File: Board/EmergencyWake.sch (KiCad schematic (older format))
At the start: 125 parts, among them J1 USB_C_Plug_USB2.0, J2 Micro_SD_Card_Det, J3 Conn_01x03, J4 Conn_01x02, J5 Conn_01x03, J6 Conn_01x04, J7 Conn_01x02, J8 Conn_01x04, J9 Conn_01x04, Q1 AO3400A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

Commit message: [Board] Added logo and changed USB plug type
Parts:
- removed J1: USB_C_Plug_USB2.0, Wuerth:632723300011, symbol Connector:USB_C_Plug_USB2.0
- added J1: USB_C_Receptacle_USB2.0, Wuerth:632723300011, symbol Connector:USB_C_Receptacle_USB2.0
- added R43: 5.1k, Resistor_SMD:R_0603_1608Metric, symbol Device:R
- R6: value 100k -> 5.1k; footprint Resistor_SMD:R_0402_1005Metric -> Resistor_SMD:R_0603_1608Metric; LCSC C25741 -> C23186
- R7: footprint Resistor_SMD:R_0402_1005Metric -> Resistor_SMD:R_0603_1608Metric; LCSC C25867 -> C22843
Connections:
- wire segments 535 -> 543
- no-connect marks 57 -> 58
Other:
- moved on the sheet: Q1, R11, R7, TP1, TP2
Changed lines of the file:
@@
 L power:GND #PWR08
 U 1 1 5E2C0277
-P 2800 5300
-F 0 "#PWR08" H 2800 5050 50  0001 C CNN
-F 1 "GND" H 2805 5127 50  0000 C CNN
-F 2 "" H 2800 5300 50  0001 C CNN
-F 3 "" H 2800 5300 50  0001 C CNN
-	1    2800 5300
+P 2800 5200
+F 0 "#PWR08" H 2800 4950 50  0001 C CNN
+F 1 "GND" H 2805 5027 50  0000 C CNN
+F 2 "" H 2800 5200 50  0001 C CNN
+F 3 "" H 2800 5200 50  0001 C CNN
+	1    2800 5200
 	1    0    0    -1
 $EndComp
@@
 L Device:Q_NMOS_GSD Q1
 U 1 1 5E31A1D8
-P 2900 4800
-F 0 "Q1" H 2750 4650 50  0000 L CNN
-F 1 "AO3400A" H 2550 4550 50  0000 L CNN
-F 2 "Package_TO_SOT_SMD:SOT-23" H 3100 4900 50  0001 C CNN
-F 3 "https://datasheet.lcsc.com/szlcsc/Alpha-Omega-Semicon-AOS-AO3400A_C20917.pdf" H 2900 4800 50  0001 C CNN
-F 4 "C20917" H 2900 4800 50  0001 C CNN "LCSC"
-	1    2900 4800
+P 2900 4700
+F 0 "Q1" H 2750 4550 50  0000 L CNN
+F 1 "AO3400A" H 2550 4450 50  0000 L CNN
+F 2 "Package_TO_SOT_SMD:SOT-23" H 3100 4800 50  0001 C CNN
+F 3 "https://datasheet.lcsc.com/szlcsc/Alpha-Omega-Semicon-AOS-AO3400A_C20917.pdf" H 2900 4700 50  0001 C CNN
+F 4 "C20917" H 2900 4700 50  0001 C CNN "LCSC"
+	1    2900 4700
 	-1   0    0    -1
 $EndComp
@@
 	2550 4100 2800 4100
 Wire Wire Line
-	2800 4100 2800 4600
+	2800 4100 2800 4500
 Wire Wire Line
-	2800 5000 2800 5200
+	2800 4900 2800 5100
 Wire Wire Line
-	2550 4400 2650 4400
+	2650 5100 2800 5100
+Connection ~ 2800 5100
 Wire Wire Line
-	2650 4400 2650 5200
-Wire Wire Line
-	2650 5200 2800 5200
-Connection ~ 2800 5200
-Wire Wire Line
-	2800 5200 2800 5300
-Wire Wire Line
-	2550 4500 4950 4500
+	2800 5100 2800 5200
 Wire Wire Line
 	2550 3900 2650 3900
@@
 $EndComp
 Wire Wire Line
-	3100 4800 3400 4800
+	3100 4700 3400 4700
 $Comp
 L power:GND #PWR03
@@
 $EndComp
 Wire Wire Line
-	2800 5200 3400 5200
+	2800 5100 3400 5100
 Wire Wire Line
-	3400 5200 3400 5150
+	3400 5100 3400 5050
 Wire Wire Line
-	3400 4850 3400 4800
-Connection ~ 3400 4800
+	3400 4750 3400 4700
+Connection ~ 3400 4700
 Wire Wire Line
-	3400 4800 4950 4800
-Text Label 4950 4800 2    50   ~ 0
+	3400 4700 4950 4700
+Text Label 4950 4700 2    50   ~ 0
 SD_EN
-Text Label 4950 4500 2    50   ~ 0
+Text Label 4950 4400 2    50   ~ 0
 SD_DET
 $Comp
@@
 L Device:R R11
 U 1 1 5E33508E
-P 3400 5000
-F 0 "R11" H 3470 5046 50  0000 L CNN
-F 1 "100k" H 3470 4955 50  0000 L CNN
-F 2 "Resistor_SMD:R_0402_1005Metric" V 3330 5000 50  0001 C CNN
-F 3 "~" H 3400 5000 50  0001 C CNN
-F 4 "C25741" H 3400 5000 50  0001 C CNN "LCSC"
-	1    3400 5000
+P 3400 4900
+F 0 "R11" H 3470 4946 50  0000 L CNN
+F 1 "100k" H 3470 4855 50  0000 L CNN
+F 2 "Resistor_SMD:R_0402_1005Metric" V 3330 4900 50  0001 C CNN
+F 3 "~" H 3400 4900 50  0001 C CNN
+F 4 "C25741" H 3400 4900 50  0001 C CNN "LCSC"
+	1    3400 4900
 	1    0    0    -1
 $EndComp
@@
 L Connector:TestPoint TP1
 U 1 1 5E3C768F
-P 1950 800
-F 0 "TP1" H 2008 918 50  0000 L CNN
-F 1 "5V in" H 2008 827 50  0000 L CNN
-F 2 "TestPoint:TestPoint_Loop_D1.80mm_Drill1.0mm_Beaded" H 2150 800 50  0001 C CNN
-F 3 "~" H 2150 800 50  0001 C CNN
-	1    1950 800
+P 2050 800
+F 0 "TP1" H 2108 918 50  0000 L CNN
+F 1 "5V in" H 2108 827 50  0000 L CNN
+F 2 "TestPoint:TestPoint_Loop_D1.80mm_Drill1.0mm_Beaded" H 2250 800 50  0001 C CNN
+F 3 "~" H 2250 800 50  0001 C CNN
+	1    2050 800
 	1    0    0    -1
 $EndComp
@@
 L Connector:TestPoint TP2
 U 1 1 5E3C8161
-P 2600 2500
-F 0 "TP2" H 2658 2618 50  0000 L CNN
-F 1 "GND in" H 2658 2527 50  0000 L CNN
-F 2 "TestPoint:TestPoint_Loop_D1.80mm_Drill1.0mm_Beaded" H 2800 2500 50  0001 C CNN
-F 3 "~" H 2800 2500 50  0001 C CNN
-	1    2600 2500
-	1    0    0    -1
-$EndComp
-$Comp
-L Connector:USB_C_Plug_USB2.0 J1
-U 1 1 5E43077B
-P 1200 1550
-F 0 "J1" H 1307 2417 50  0000 C CNN
-F 1 "USB_C_Plug_USB2.0" H 1307 2326 50  0000 C CNN
-F 2 "Wuerth:632723300011" H 1350 1550 50  0001 C CNN
-F 3 "https://www.we-online.de/katalog/datasheet/632723300011.pdf" H 1350 1550 50  0001 C CNN
-F 4 "632723300011" H 1200 1550 50  0001 C CNN "Würth"
-	1    1200 1550
+P 2750 2500
+F 0 "TP2" H 2808 2618 50  0000 L CNN
+F 1 "GND in" H 2808 2527 50  0000 L CNN
+F 2 "TestPoint:TestPoint_Loop_D1.80mm_Drill1.0mm_Beaded" H 2950 2500 50  0001 C CNN
+F 3 "~" H 2950 2500 50  0001 C CNN
+	1    2750 2500
 	1    0    0    -1
 $EndComp
-NoConn ~ 1800 1250
 $Comp
 L Device:R R6
@@
 P 1950 1900
 F 0 "R6" H 2020 1946 50  0000 L CNN
-F 1 "100k" H 2020 1855 50  0000 L CNN
-F 2 "Resistor_SMD:R_0402_1005Metric" V 1880 1900 50  0001 C CNN
+F 1 "5.1k" H 2020 1855 50  0000 L CNN
+F 2 "Resistor_SMD:R_0603_1608Metric" V 1880 1900 50  0001 C CNN
 F 3 "~" H 1950 1900 50  0001 C CNN
-F 4 "C25741" H 1950 1900 50  0001 C CNN "LCSC"
+F 4 "C23186" H 1950 1900 50  0001 C CNN "LCSC"
 	1    1950 1900
 	1    0    0    -1
@@
 Connection ~ 3150 850
 Wire Wire Line
-	2500 950  1950 950
+	2500 950  2050 950
 Wire Wire Line
 	3150 1500 3150 2500
 Wire Wire Line
-	3150 2500 2600 2500
+	3150 2500 2750 2500
 Connection ~ 1950 2500
 Wire Wire Line
-	1800 1450 2950 1450
+	1800 1450 1850 1450
 Wire Wire Line
-	1800 1650 2350 1650
+	1800 1650 1850 1650
 Wire Wire Line
 	1200 2500 1700 2500
@@
 	1700 2500 1950 2500
 Wire Wire Line
-	1950 800  1950 950
+	2050 800  2050 950
 Wire Wire Line
 	2900 850  3150 850
-Connection ~ 1950 950
+Connection ~ 2050 950
 Wire Wire Line
-	1950 950  1800 950
-Connection ~ 2600 2500
+	2050 950  1800 950
+Connection ~ 2750 2500
 Wire Wire Line
-	2600 2500 1950 2500
+	2750 2500 2250 2500
 Text Label 2950 1650 2    50   ~ 0
 USB_DP
@@
 L Device:R R7
 U 1 1 5EAA5F48
-P 2350 1900
-F 0 "R7" H 2420 1946 50  0000 L CNN
-F 1 "1.5k" H 2420 1855 50  0000 L CNN
-F 2 "Resistor_SMD:R_0402_1005Metric" V 2280 1900 50  0001 C CNN
-F 3 "~" H 2350 1900 50  0001 C CNN
-F 4 "C25867" H 2350 1900 50  0001 C CNN "LCSC"
-	1    2350 1900
+P 2550 1900
+F 0 "R7" H 2620 1946 50  0000 L CNN
+F 1 "1.5k" H 2620 1855 50  0000 L CNN
+F 2 "Resistor_SMD:R_0603_1608Metric" V 2480 1900 50  0001 C CNN
+F 3 "~" H 2550 1900 50  0001 C CNN
+F 4 "C22843" H 2550 1900 50  0001 C CNN "LCSC"
+	1    2550 1900
 	1    0    0    -1
 $EndComp
 Wire Wire Line
-	2350 1750 2350 1650
-Connection ~ 2350 1650
+	2550 1750 2550 1650
+Connection ~ 2550 1650
 Wire Wire Line
-	2350 1650 2950 1650
+	2550 1650 2950 1650
 $Comp
 L power:VCC #PWR06
 U 1 1 5EADF0A8
-P 2350 2100
-F 0 "#PWR06" H 2350 1950 50  0001 C CNN
-F 1 "VCC" H 2367 2273 50  0000 C CNN
-F 2 "" H 2350 2100 50  0001 C CNN
-F 3 "" H 2350 2100 50  0001 C CNN
-	1    2350 2100
+P 2550 2100
+F 0 "#PWR06" H 2550 1950 50  0001 C CNN
+F 1 "VCC" H 2550 2250 50  0000 C CNN
+F 2 "" H 2550 2100 50  0001 C CNN
+F 3 "" H 2550 2100 50  0001 C CNN
+	1    2550 2100
 	-1   0    0    1
 $EndComp
 Wire Wire Line
-	2350 2050 2350 2100
+	2550 2050 2550 2100
 $Comp
 L power:+5V #PWR021
@@
 Connection ~ 10800 1050
 Wire Wire Line
-	9250 1950 10100 1950
-Wire Wire Line
 	10800 1950 10800 1850
 Wire Wire Line
-	10300 1800 10300 1950
-Connection ~ 10300 1950
-Wire Wire Line
-	10300 1950 10800 1950
-Wire Wire Line
-	10100 1800 10100 1950
-Connection ~ 10100 1950
+	10200 1800 10200 1950
+Connection ~ 10200 1950
 Wire Wire Line
-	10100 1950 10300 1950
+	10200 1950 10800 1950
 Wire Wire Line
 	9250 1850 9250 1950
@@
 	1    0    0    -1
 $EndComp
+Wire Wire Line
+	9250 1950 10200 1950
+Wire Wire Line
+	2550 4500 2650 4500
+Wire Wire Line
+	2650 4500 2650 5100
+Wire Wire Line
+	4950 4400 2550 4400
+$Comp
+L Connector:USB_C_Receptacle_USB2.0 J1
+U 1 1 5E98AED3
+P 1200 1550
+F 0 "J1" H 1307 2417 50  0000 C CNN
+F 1 "USB_C_Receptacle_USB2.0" H 1307 2326 50  0000 C CNN
+F 2 "Wuerth:632723300011" H 1350 1550 50  0001 C CNN
+F 3 "https://www.usb.org/sites/default/files/documents/usb_type-c.zip" H 1350 1550 50  0001 C CNN
+	1    1200 1550
+	1    0    0    -1
+$EndComp
+Wire Wire Line
+	1800 1550 1850 1550
+Wire Wire Line
+	1850 1550 1850 1450
+Connection ~ 1850 1450
+Wire Wire Line
+	1850 1450 2950 1450
+Wire Wire Line
+	1800 1750 1850 1750
+Wire Wire Line
+	1850 1750 1850 1650
+Connection ~ 1850 1650
+Wire Wire Line
+	1850 1650 2550 1650
+$Comp
+L Device:R R43
+U 1 1 5EB8A4F4
+P 2250 1900
+F 0 "R43" H 2320 1946 50  0000 L CNN
+F 1 "5.1k" H 2320 1855 50  0000 L CNN
+F 2 "Resistor_SMD:R_0603_1608Metric" V 2180 1900 50  0001 C CNN
+F 3 "~" H 2250 1900 50  0001 C CNN
+F 4 "C23186" H 2250 1900 50  0001 C CNN "LCSC"
+	1    2250 1900
+	1    0    0    -1
+$EndComp
+Wire Wire Line
+	2250 1750 2250 1250
+Wire Wire Line
+	2250 1250 1800 1250
+Wire Wire Line
+	2250 2050 2250 2500
+Connection ~ 2250 2500
+Wire Wire Line
+	2250 2500 1950 2500
+NoConn ~ 1800 2050
+NoConn ~ 1800 2150
 $EndSCHEMATC

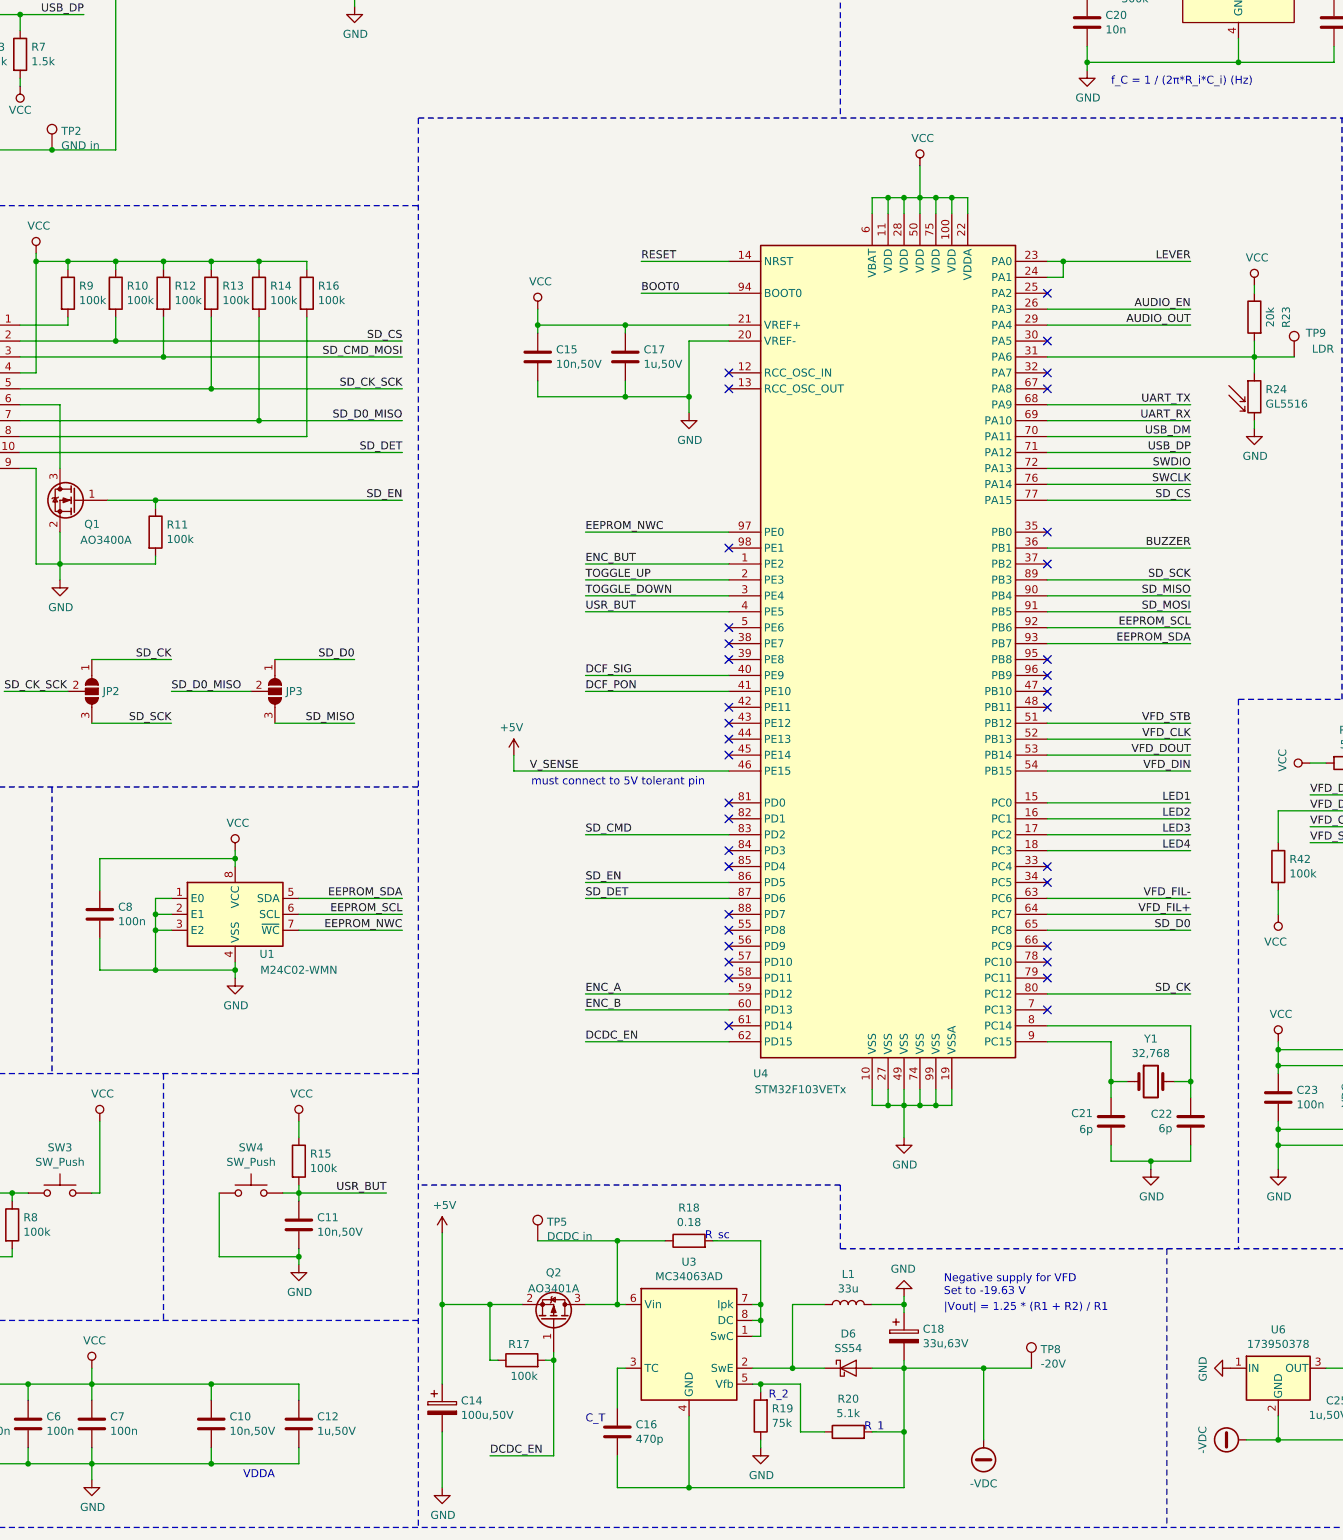
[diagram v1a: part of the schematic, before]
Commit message: [Board] Added GNDD and routed DCDC converter
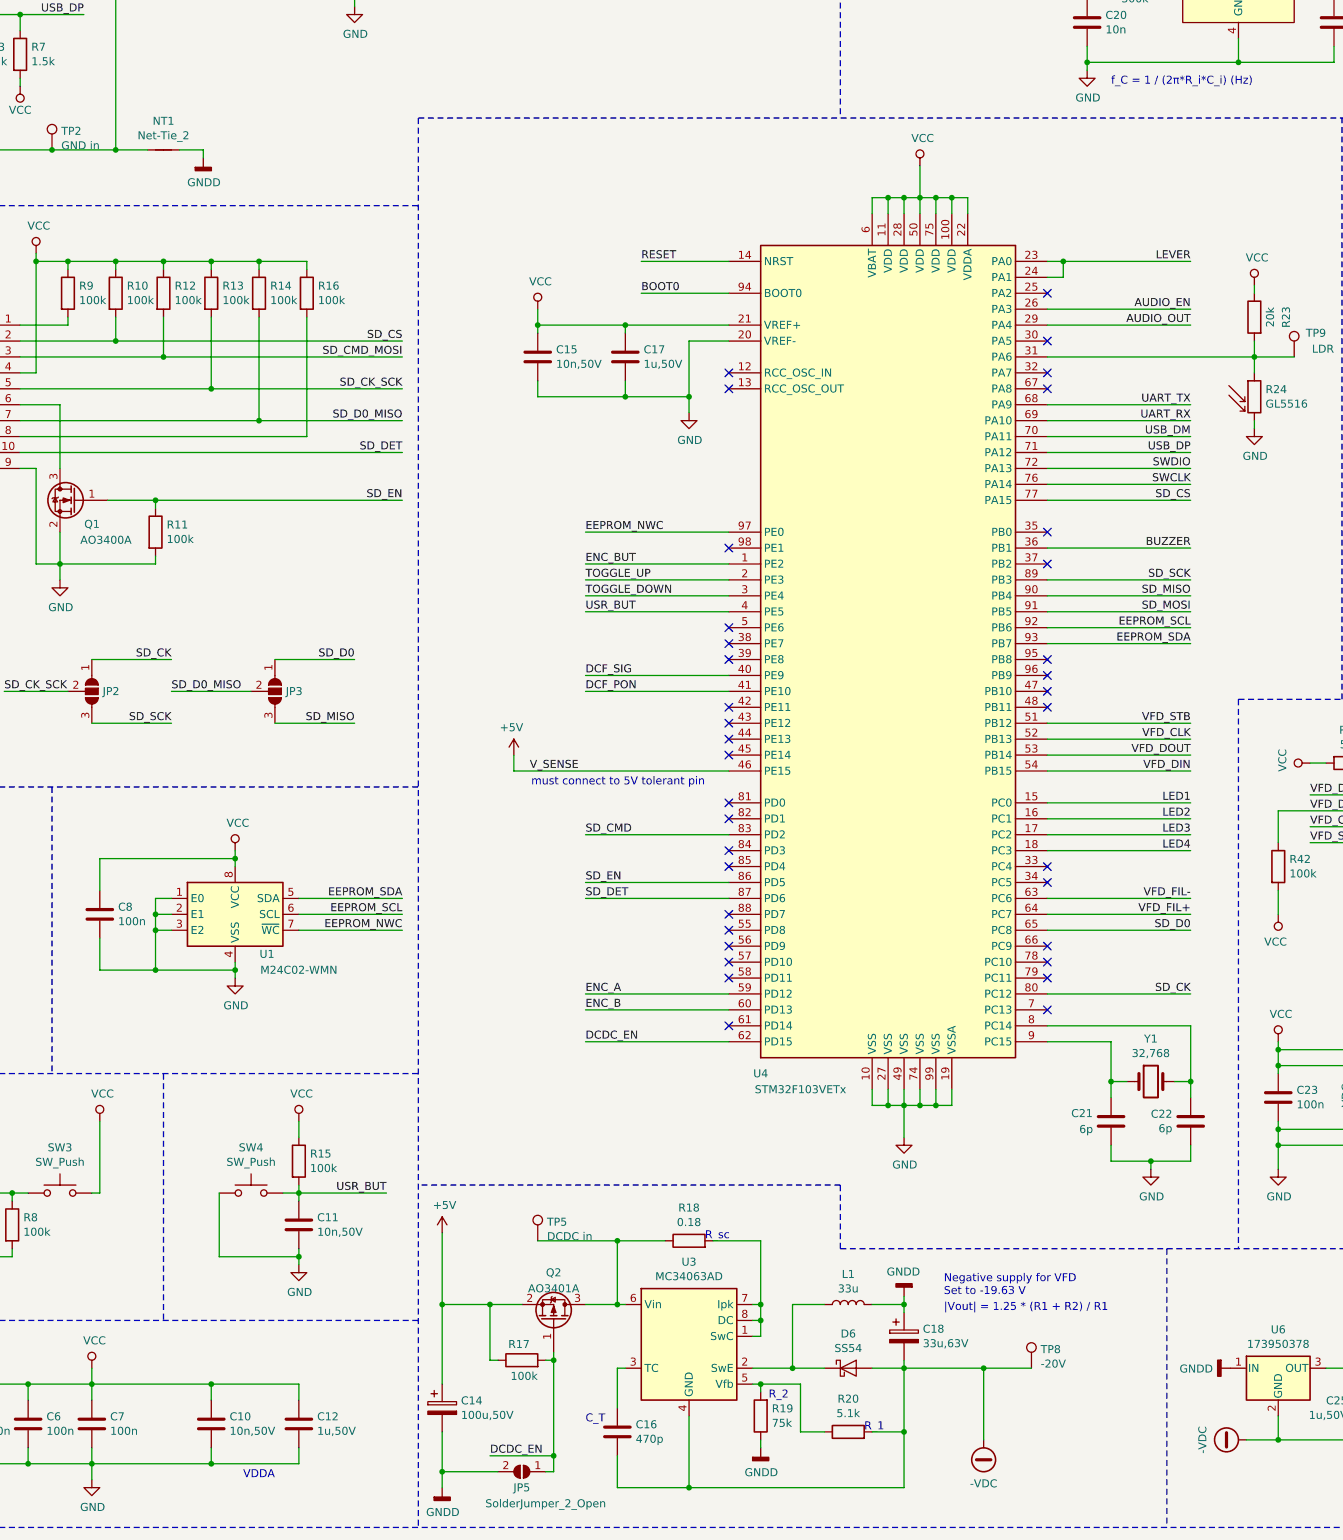
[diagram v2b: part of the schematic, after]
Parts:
- added JP5: SolderJumper_2_Open, Jumper:SolderJumper-2_P1.3mm_Open_TrianglePad1.0x1.5mm, symbol Jumper:SolderJumper_2_Open
- added NT1: Net-Tie_2, NetTie:NetTie-2_SMD_Pad2.0mm, symbol Device:Net-Tie_2
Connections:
- net DCDC_EN: now also JP5.1 (A)
- net GND: now also NT1.1; no longer C14.2, C18.1, L1.2, R19.1, U6.1 (IN)
- new net GNDD: C14.2, C18.1, JP5.2 (B), L1.2, NT1.2, R19.1, U6.1 (IN)
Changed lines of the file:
@@
-$EndComp
-$Comp
-L power:GND #PWR020
-U 1 1 5E40EC79
-P 5200 10900
-F 0 "#PWR020" H 5200 10650 50  0001 C CNN
-F 1 "GND" H 5205 10727 50  0000 C CNN
-F 2 "" H 5200 10900 50  0001 C CNN
-F 3 "" H 5200 10900 50  0001 C CNN
-	1    5200 10900
-	1    0    0    -1
 $EndComp
 $Comp
@@
 	6300 10150 6300 10400
 Wire Wire Line
-	5200 10550 5200 10900
+	5200 10550 5200 10800
 Wire Wire Line
 	7900 10150 8100 10150
 Connection ~ 8100 10150
-$Comp
-L power:GND #PWR027
-U 1 1 5E9D71E2
-P 8100 9700
-F 0 "#PWR027" H 8100 9450 50  0001 C CNN
-F 1 "GND" H 8105 9527 50  0000 C CNN
-F 2 "" H 8100 9700 50  0001 C CNN
-F 3 "" H 8100 9700 50  0001 C CNN
-	1    8100 9700
-	-1   0    0    1
-$EndComp
 Connection ~ 7400 10150
 Wire Wire Line
@@
 Wire Wire Line
 	7200 10250 7150 10250
-$Comp
-L power:GND #PWR025
-U 1 1 5EFF3756
-P 7200 10650
-F 0 "#PWR025" H 7200 10400 50  0001 C CNN
-F 1 "GND" H 7205 10477 50  0000 C CNN
-F 2 "" H 7200 10650 50  0001 C CNN
-F 3 "" H 7200 10650 50  0001 C CNN
-	1    7200 10650
-	1    0    0    -1
-$EndComp
 Wire Wire Line
 	7200 10600 7200 10650
@@
 V_drive is 3.3 V\nabove -VDC
 $Comp
-L power:GND #PWR032
-U 1 1 5E448B6E
-P 10150 10150
-F 0 "#PWR032" H 10150 9900 50  0001 C CNN
-F 1 "GND" H 10155 9977 50  0000 C CNN
-F 2 "" H 10150 10150 50  0001 C CNN
-F 3 "" H 10150 10150 50  0001 C CNN
-	1    10150 10150
-	0    1    1    0
-$EndComp
-$Comp
 L power:-VDC #PWR033
 U 1 1 5E4483D8
@@
 NoConn ~ 1800 2050
 NoConn ~ 1800 2150
+$Comp
+L Jumper:SolderJumper_2_Open JP5
+U 1 1 5E45A9FA
+P 5700 10800
+F 0 "JP5" H 5700 10700 50  0000 C CNN
+F 1 "SolderJumper_2_Open" H 5550 10600 50  0000 C CNN
+F 2 "Jumper:SolderJumper-2_P1.3mm_Open_TrianglePad1.0x1.5mm" H 5700 10800 50  0001 C CNN
+F 3 "~" H 5700 10800 50  0001 C CNN
+	1    5700 10800
+	-1   0    0    -1
+$EndComp
+Wire Wire Line
+	5900 10700 5900 10800
+Wire Wire Line
+	5900 10800 5850 10800
+Connection ~ 5900 10700
+Wire Wire Line
+	5550 10800 5200 10800
+Connection ~ 5200 10800
+Wire Wire Line
+	5200 10800 5200 10900
+$Comp
+L power:GNDD #PWR032
+U 1 1 5E55B5E3
+P 8100 9700
+F 0 "#PWR032" H 8100 9450 50  0001 C CNN
+F 1 "GNDD" H 8104 9545 50  0000 C CNN
+F 2 "" H 8100 9700 50  0001 C CNN
+F 3 "" H 8100 9700 50  0001 C CNN
+	1    8100 9700
+	-1   0    0    1
+$EndComp
+$Comp
+L power:GNDD #PWR027
+U 1 1 5E567DAC
+P 7200 10650
+F 0 "#PWR027" H 7200 10400 50  0001 C CNN
+F 1 "GNDD" H 7204 10495 50  0000 C CNN
+F 2 "" H 7200 10650 50  0001 C CNN
+F 3 "" H 7200 10650 50  0001 C CNN
+	1    7200 10650
+	1    0    0    -1
+$EndComp
+$Comp
+L power:GNDD #PWR025
+U 1 1 5E569466
+P 5200 10900
+F 0 "#PWR025" H 5200 10650 50  0001 C CNN
+F 1 "GNDD" H 5204 10745 50  0000 C CNN
+F 2 "" H 5200 10900 50  0001 C CNN
+F 3 "" H 5200 10900 50  0001 C CNN
+	1    5200 10900
+	1    0    0    -1
+$EndComp
+$Comp
+L power:GNDD #PWR073
+U 1 1 5E56C0BF
+P 10150 10150
+F 0 "#PWR073" H 10150 9900 50  0001 C CNN
+F 1 "GNDD" V 10154 10040 50  0000 R CNN
+F 2 "" H 10150 10150 50  0001 C CNN
+F 3 "" H 10150 10150 50  0001 C CNN
+	1    10150 10150
+	0    1    1    0
+$EndComp
+$Comp
+L power:GNDD #PWR020
+U 1 1 5E57A04B
+P 3700 2550
+F 0 "#PWR020" H 3700 2300 50  0001 C CNN
+F 1 "GNDD" H 3704 2395 50  0000 C CNN
+F 2 "" H 3700 2550 50  0001 C CNN
+F 3 "" H 3700 2550 50  0001 C CNN
+	1    3700 2550
+	1    0    0    -1
+$EndComp
+$Comp
+L Device:Net-Tie_2 NT1
+U 1 1 5E5849C3
+P 3450 2500
+F 0 "NT1" H 3450 2681 50  0000 C CNN
+F 1 "Net-Tie_2" H 3450 2590 50  0000 C CNN
+F 2 "NetTie:NetTie-2_SMD_Pad2.0mm" H 3450 2500 50  0001 C CNN
+F 3 "~" H 3450 2500 50  0001 C CNN
+	1    3450 2500
+	1    0    0    -1
+$EndComp
+Wire Wire Line
+	3550 2500 3700 2500
+Wire Wire Line
+	3700 2500 3700 2550
+Wire Wire Line
+	3350 2500 3150 2500
+Connection ~ 3150 2500
 $EndSCHEMATC
